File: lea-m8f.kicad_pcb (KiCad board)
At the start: 2 copper layers, 27 parts, among them CON1 USB-MICRO-B, J1 RF_IN, J2 DB9, J3 PPS, J4 30.72, P1 CONN_01X08, U100 B200_GPSDO, U2 MAX232, U3 LEA-M8F, U4 NC7SZ125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

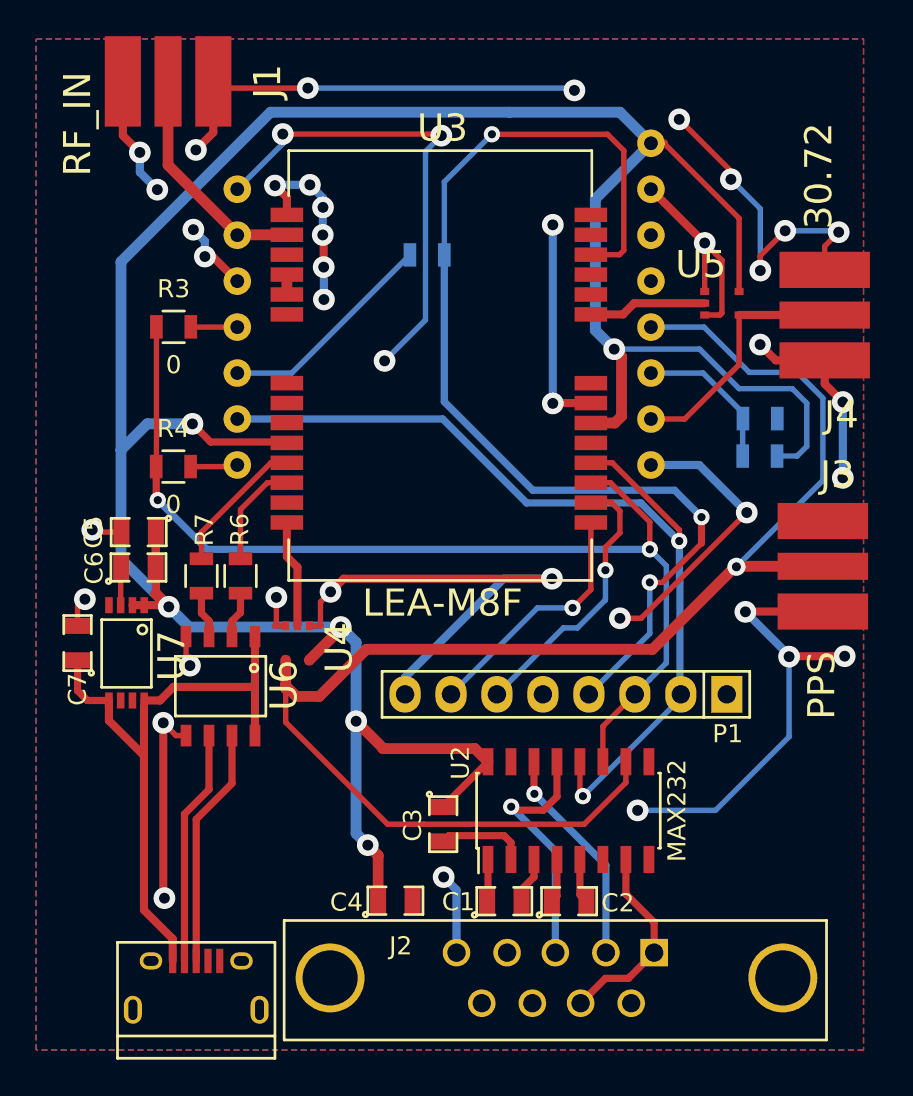
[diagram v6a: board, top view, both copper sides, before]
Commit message: Correct margin on the left
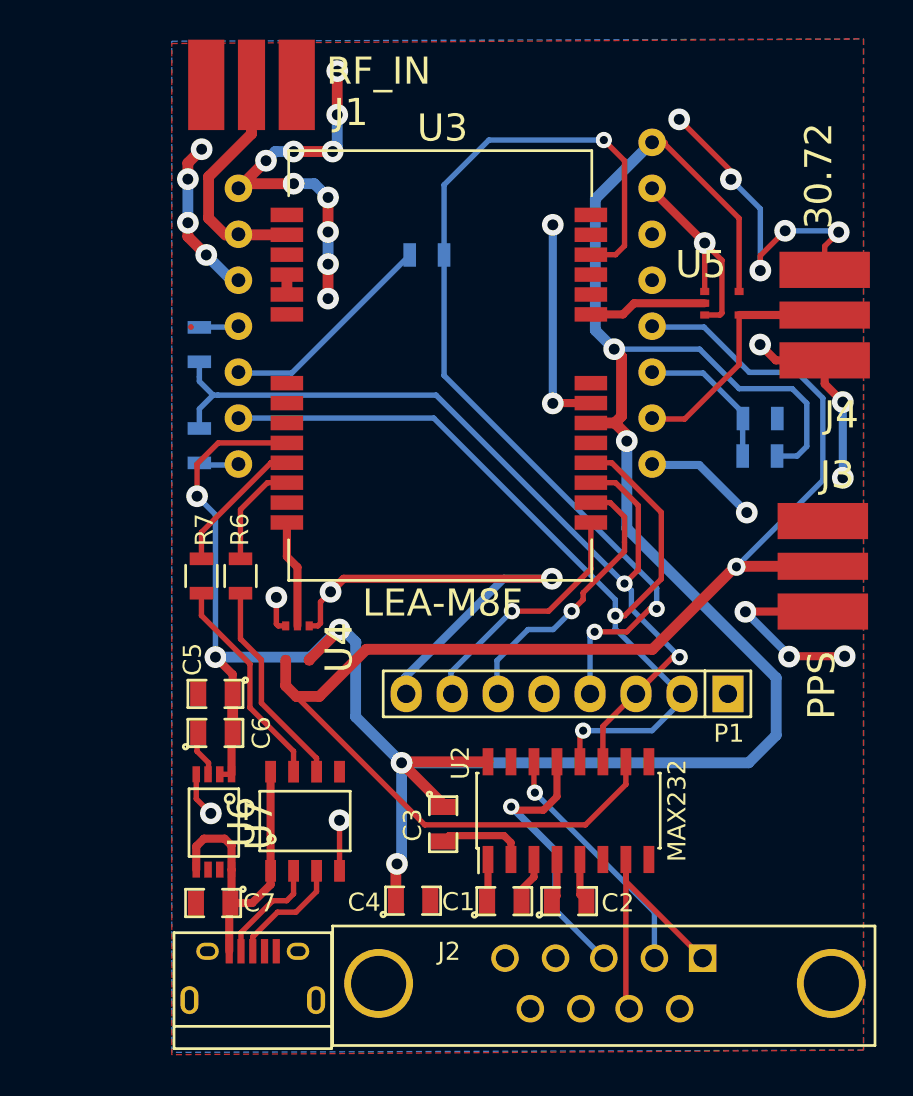
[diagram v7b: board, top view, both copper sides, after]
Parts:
- R3, R4: moved to B.Cu
- moved C7 16.2 mm to (182.8, 108.2), turned to 180 degrees
- moved U6 13.0 mm to (186.0, 106.4), turned to 90 degrees
- moved U7 10.5 mm to (183.8, 101.1)
- moved C6 10.1 mm to (182.9, 98.8)
- moved C5 9.90 mm to (182.9, 96.6)
- moved J1 4.61 mm to (182.4, 63.0)
- moved CON1 3.17 mm to (183.7, 110.8)
- moved J2 2.70 mm to (204.4, 112.7)
- moved R4 1.84 mm to (182.0, 82.9), turned to 270 degrees
- moved R3 1.73 mm to (182.0, 77.3), turned to 90 degrees
- moved C4 0.98 mm to (193.8, 108.0)
- moved U100 0.08 mm to (196.9, 73.7)
- moved P1 0.07 mm to (202.3, 96.6)
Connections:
- U6 pad 2: Net-(R6-Pad1) -> Net-(CON1-Pad2)
- U6 pad 3: Net-(R7-Pad1) -> Net-(CON1-Pad3)
- U6 pad 6: Net-(CON1-Pad2) -> Net-(R6-Pad1)
- U6 pad 7: Net-(CON1-Pad3) -> Net-(R7-Pad1)
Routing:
- net GND: track 216.7 -> 135.7 mm, vias 42 -> 34
- net /5VUSB: track 34.8 -> 18.3 mm
- net Net-(R7-Pad1): track 2.56 -> 12.0 mm
- net Net-(R6-Pad1): track 2.58 -> 11.6 mm
- net VCC: track 158.1 -> 149.1 mm, vias 6 -> 7
- net Net-(CON1-Pad2): track 13.0 -> 6.08 mm
- net Net-(CON1-Pad3): track 13.3 -> 6.48 mm
- net /SB_N: track 60.6 -> 54.0 mm
- net /TXD: track 57.2 -> 52.2 mm
- net Net-(J2-Pad1): track 11.0 -> 15.5 mm
- net /PPS_BUFF: track 82.5 -> 80.3 mm
- net Net-(J2-Pad3): track 13.9 -> 15.3 mm
- net Net-(J2-Pad2): track 12.2 -> 13.6 mm
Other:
- net class Power: trace_width 0.45 -> 0.6

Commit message: update PCB
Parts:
- moved J1 11.2 mm to (179.4, 73.7), turned to 180 degrees
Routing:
- net GND: track 135.7 -> 115.3 mm, vias 34 -> 25
- net /RF_IN: track 13.0 -> 7.65 mm
